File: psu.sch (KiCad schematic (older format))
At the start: 55 parts, among them J1 Screw_Terminal_01x02, J2 Barrel_Jack, J3 Conn_01x02, SW1 SW_SP4T, SW2 SW_SP4T, SW3 SW_SPST, U1 LM4040DBZ-2.5, U2 LT3081, U3 LM358, U4 LM334M, U5 LM317L_TO92, U6 LM317L_TO92

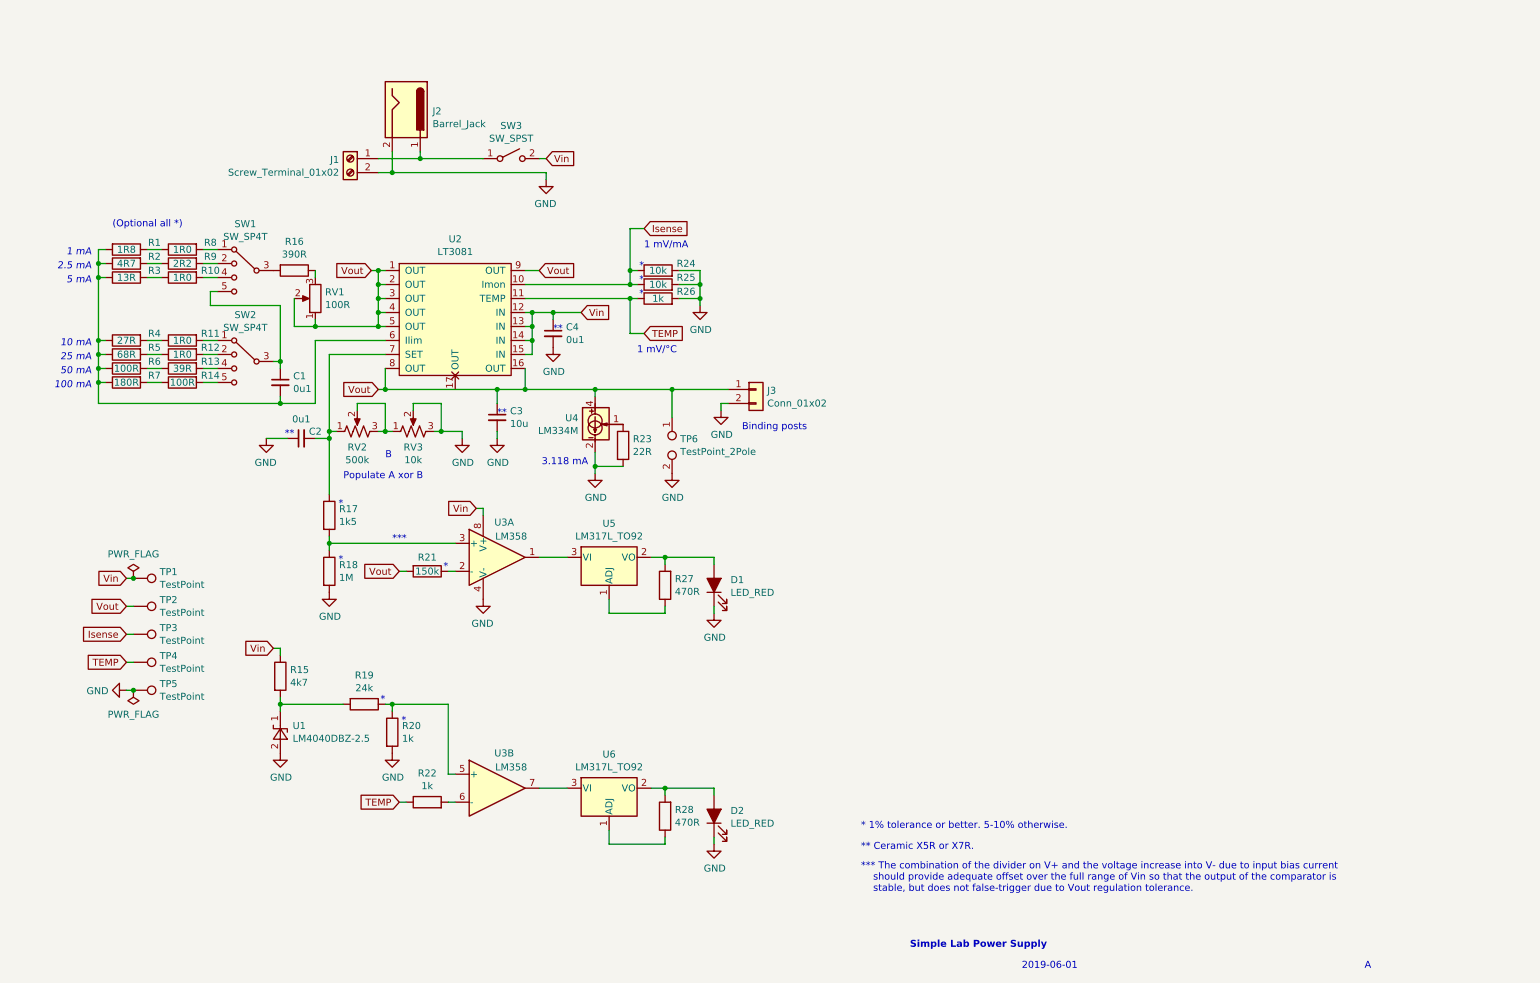
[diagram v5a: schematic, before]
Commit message: Finished footprints
Also decided to use a comparator instead of the LM358 (would not handle inputs above Vin).
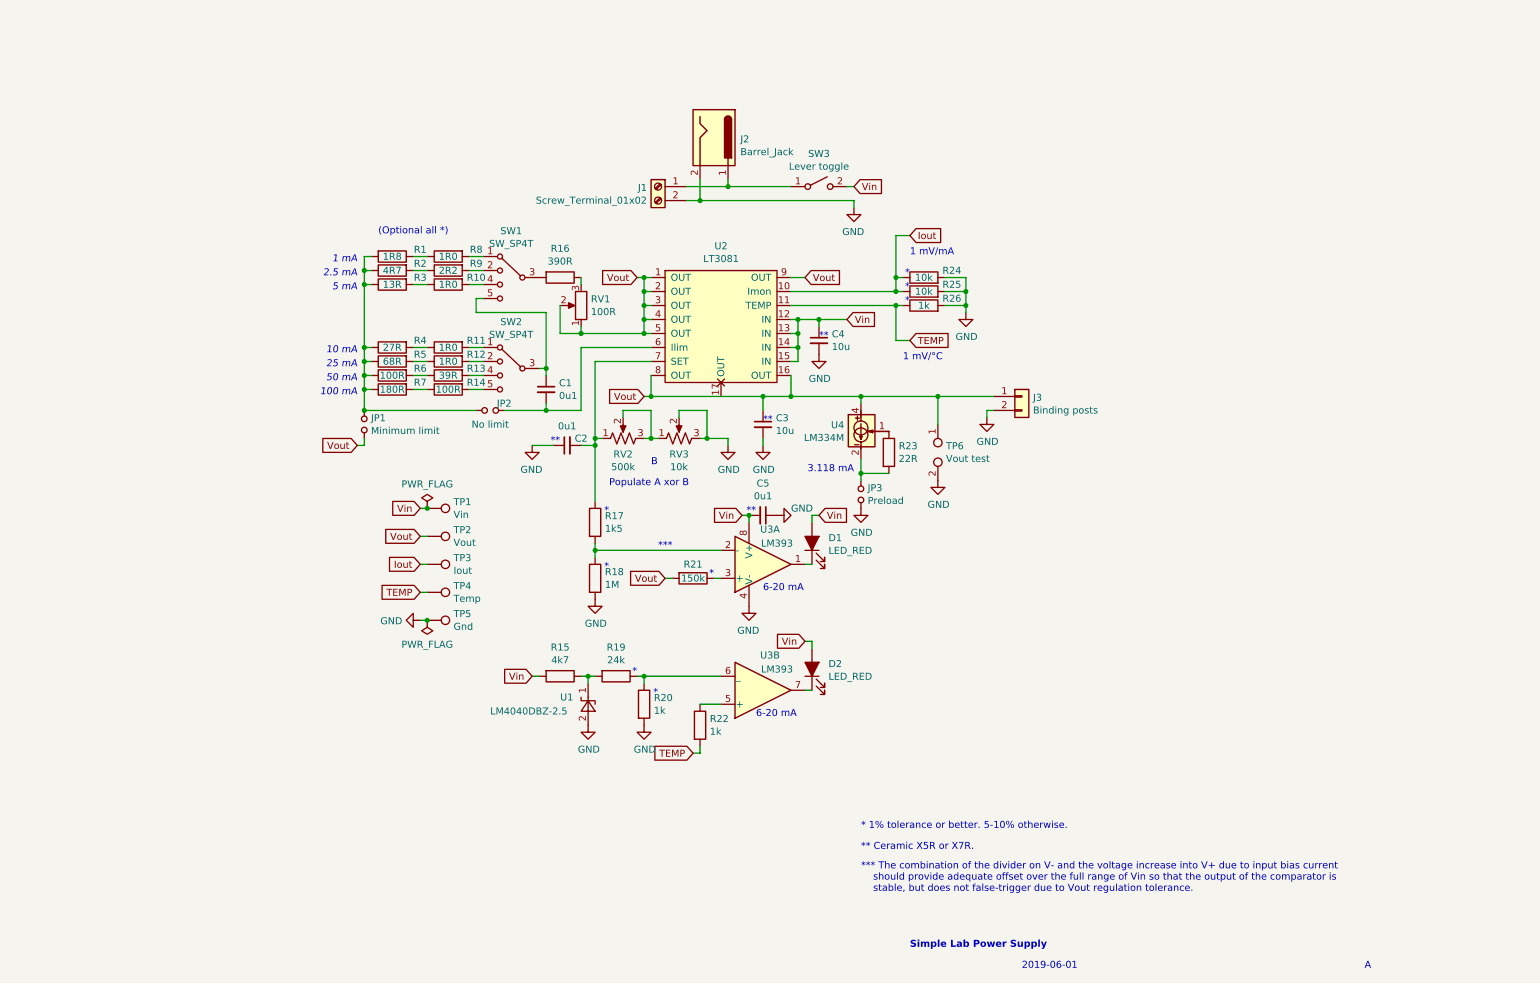
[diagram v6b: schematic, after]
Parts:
- removed R27, R28: 470R, Resistor_THT:R_Axial_DIN0207_L6.3mm_D2.5mm_P10.16mm_Horizontal, symbol Device:R
- removed U3: LM358, Package_SO:SOIC-8_3.9x4.9mm_P1.27mm, symbol Amplifier_Operational:LM358
- removed U5, U6: LM317L_TO92, Package_TO_SOT_THT:TO-92_Inline, symbol Regulator_Linear:LM317L_TO92
- added C5: 0u1, Capacitor_THT:C_Disc_D5.0mm_W2.5mm_P2.50mm, symbol Device:C_Small
- added JP1: Minimum limit, Connector_PinHeader_2.54mm:PinHeader_1x02_P2.54mm_Vertical, symbol Device:Jumper_NO_Small
- added JP2: No limit, Connector_PinHeader_2.54mm:PinHeader_1x02_P2.54mm_Vertical, symbol Device:Jumper_NO_Small
- added JP3: Preload, Connector_PinHeader_2.54mm:PinHeader_1x02_P2.54mm_Vertical, symbol Device:Jumper_NO_Small
- added U3: LM393, Package_SO:SOIC-8_3.9x4.9mm_P1.27mm, symbol Comparator:LM393
- C4: value 0u1 -> 10u; footprint Capacitor_THT:C_Disc_D5.0mm_W2.5mm_P2.50mm -> Capacitor_SMD:C_1206_3216Metric_Pad1.42x1.75mm_HandSolder
- J3: value Conn_01x02 -> Binding posts; footprint (none) -> psu-foot:Binding Posts
- SW1, SW2: footprint (none) -> psu-foot:SP4T_CK_SK-14D01-G-6
- SW3: value SW_SPST -> Lever toggle; footprint (none) -> psu-foot:SW_SPST_Lever_Rubber
- TP1: value TestPoint -> Vin
- TP2: value TestPoint -> Vout
- TP3: value TestPoint -> Iout
- TP4: value TestPoint -> Temp
- TP5: value TestPoint -> Gnd
- TP6: value TestPoint_2Pole -> Vout test
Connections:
- net GND: now also C5.1, JP3.2, U3.4 (V-); no longer D1.1 (K), D2.1 (K), R23.2, U4.2, U4.3, U4.6, U4.7
- net TEMP: now also R22.2; no longer R22.1
- net Vin: now also D1.2 (A), D2.2 (A), R15.2, C5.2, U3.8 (V+); no longer R15.1
- net Vout: now also JP1.2
- net at R1.2, R2.1, R3.1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: now also JP1.1, JP2.2; no longer C1.2, U2.6 (Ilim)
- net at R17.2, R18.1: now also U3.2 (-)
- net at R21.1: now also U3.3 (+)
- net at R19.2, U1.1 (K): now also R15.1; no longer R15.2
- net at R19.1, R20.1: now also U3.6 (_)
- net Isense renamed Iout
- new net: C1.2, JP2.1, U2.6 (Ilim)
- new net: JP3.1, R23.2, U4.2, U4.3, U4.6, U4.7
- new net: D1.1 (K), U3.1
- new net: D2.1 (K), U3.7
- new net: R22.1, U3.5 (+)
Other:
- note added: "*** The combination of the divider on V- and the voltage increase into V+ due to input bias current\n should provide adequate offset over the full range of Vin so that the output of the comparator is\n stable, but does not false-trigger due to Vout regulation tolerance."
- note added: "6-20 mA"
- note removed: "*** The combination of the divider on V+ and the voltage increase into V- due to input bias current\n should provide adequate offset over the full range of Vin so that the output of the comparator is\n stable, but does not false-trigger due to Vout regulation tolerance."
- note removed: "Binding posts"
- moved on the sheet: C1, C2, C3, C4, D1, D2, J1, J2, J3, R1, R10, R11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

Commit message: Started routing
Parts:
- RV1: footprint Potentiometer_THT:Potentiometer_Piher_PC-16_Single_Horizontal -> psu-foot:Trim_pot_Bourns_TC33X-2-101E
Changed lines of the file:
@@
 F 0 "RV1" H 4930 2854 50  0000 R CNN
 F 1 "100R" H 4930 2945 50  0000 R CNN
-F 2 "Potentiometer_THT:Potentiometer_Piher_PC-16_Single_Horizontal" H 5000 2900 50  0001 C CNN
+F 2 "psu-foot:Trim_pot_Bourns_TC33X-2-101E" H 5000 2900 50  0001 C CNN
 F 3 "~" H 5000 2900 50  0001 C CNN
 	1    5000 2900

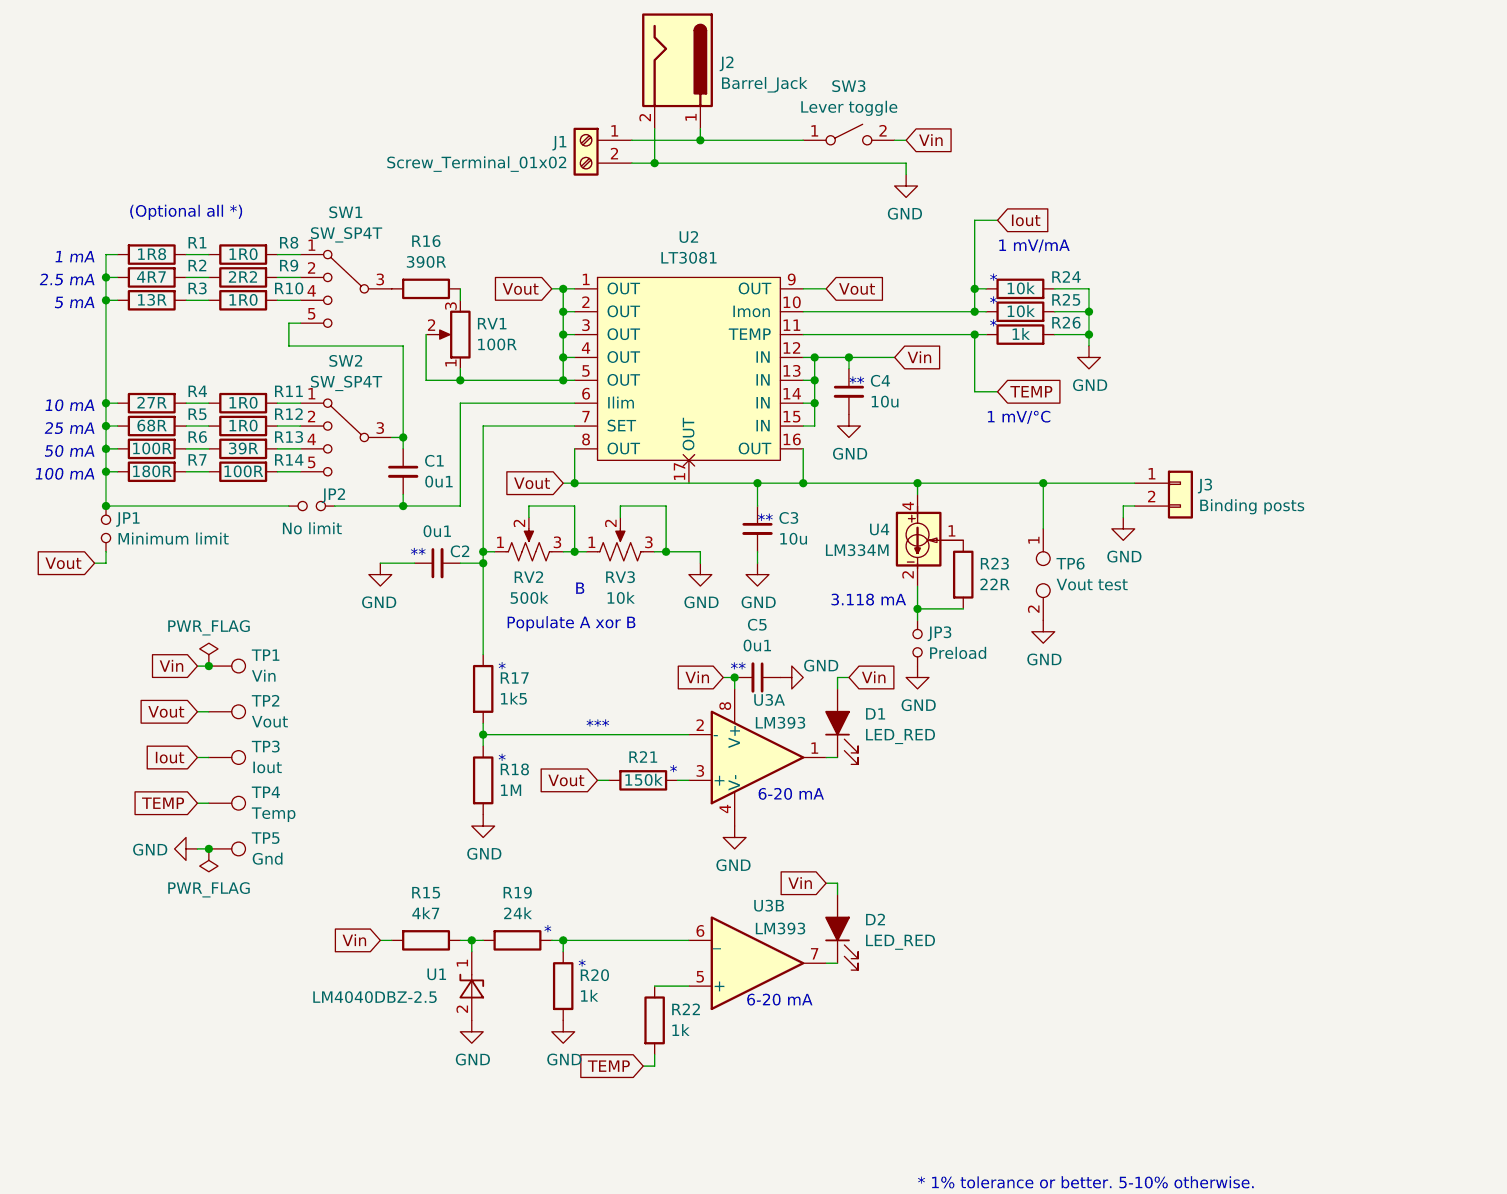
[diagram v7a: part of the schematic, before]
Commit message: Minor schematic tweaks; more routing
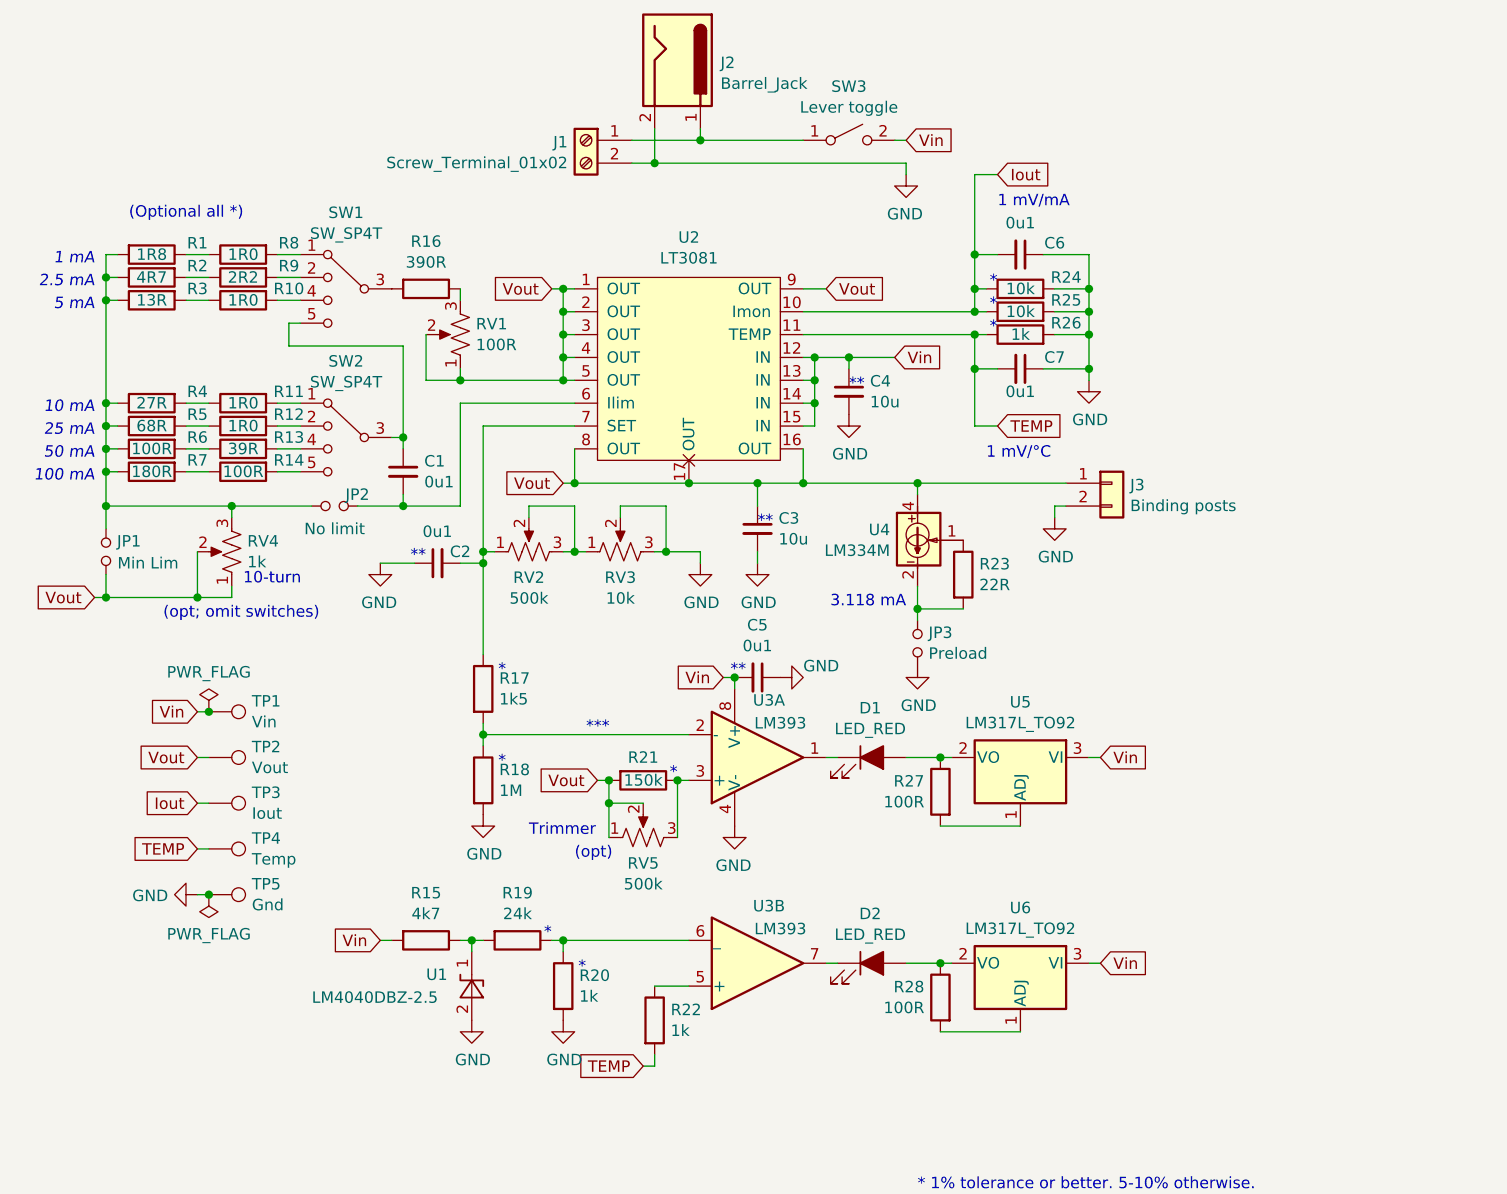
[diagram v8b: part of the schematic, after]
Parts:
- removed RV1: 100R, psu-foot:Trim_pot_Bourns_TC33X-2-101E, symbol Device:R_POT
- removed TP6: Vout test, TestPoint:TestPoint_2Pads_Pitch5.08mm_Drill1.3mm, symbol Connector:TestPoint_2Pole
- added C6, C7: 0u1, Capacitor_THT:C_Disc_D5.0mm_W2.5mm_P2.50mm, symbol Device:C_Small
- added R27, R28: 100R, Resistor_THT:R_Axial_DIN0207_L6.3mm_D2.5mm_P10.16mm_Horizontal, symbol Device:R
- added RV1: 100R, psu-foot:Trim_pot_Bourns_TC33X-2-101E, symbol Device:R_POT_US
- added RV4: 1k, Potentiometer_THT:Potentiometer_Piher_PC-16_Single_Horizontal, symbol Device:R_POT_US
- added RV5: 500k, psu-foot:Trim_pot_Bourns_TC33X-2-101E, symbol Device:R_POT_US
- added U5, U6: LM317L_TO92, Package_TO_SOT_THT:TO-92_Inline, symbol Regulator_Linear:LM317L_TO92
- D1, D2: footprint LED_THT:LED_D5.0mm -> LED_THT:LED_D3.0mm
- JP1: value Minimum limit -> Min Lim
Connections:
- net GND: now also C6.1, C7.1
- net Iout: now also C6.2
- net TEMP: now also C7.2
- net Vin: now also U5.3 (VI), U6.3 (VI); no longer D1.2 (A), D2.2 (A)
- net Vout: now also U2.17 (OUT), RV1.1, RV1.2, RV4.1, RV4.2, RV5.1, RV5.2
- net at JP1.1, JP2.2, R1.2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: now also RV4.3
- net at R21.1, U3.3 (+): now also RV5.3
- net at R16.1: now also RV1.3
- new net: R27.2, U5.1 (ADJ)
- new net: D1.2 (A), R27.1, U5.2 (VO)
- new net: R28.2, U6.1 (ADJ)
- new net: D2.2 (A), R28.1, U6.2 (VO)
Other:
- note added: "(opt)"
- note added: "(opt; omit switches)"
- note added: "10-turn"
- note added: "Trimmer"
- note removed: "6-20 mA"
- note removed: "B"
- note removed: "Populate A xor B"
- moved on the sheet: J3, JP1, JP2, TP1, TP2, TP3, TP4, TP5
